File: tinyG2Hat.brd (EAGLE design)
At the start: 101.9 x 69.3 mm, 31 parts

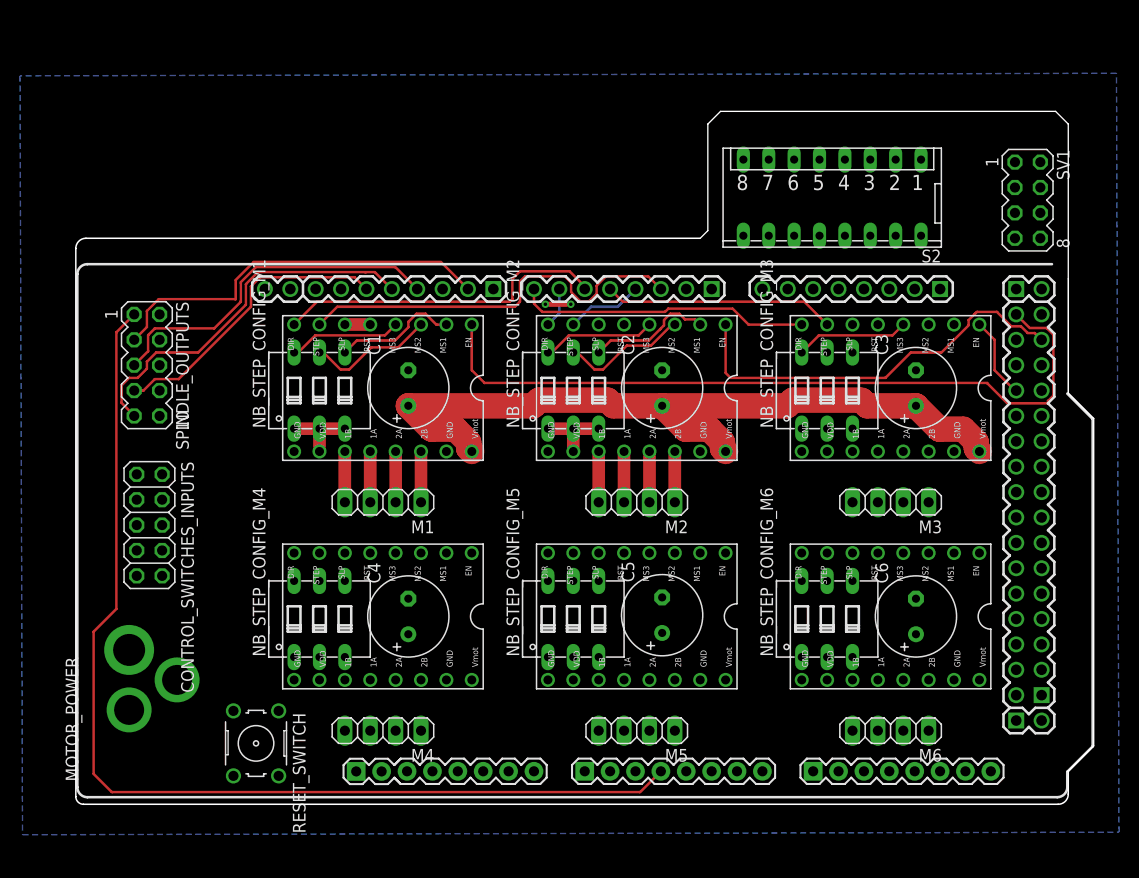
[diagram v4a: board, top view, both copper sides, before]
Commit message: Routage de M3 et des entrées avec leur switch de config
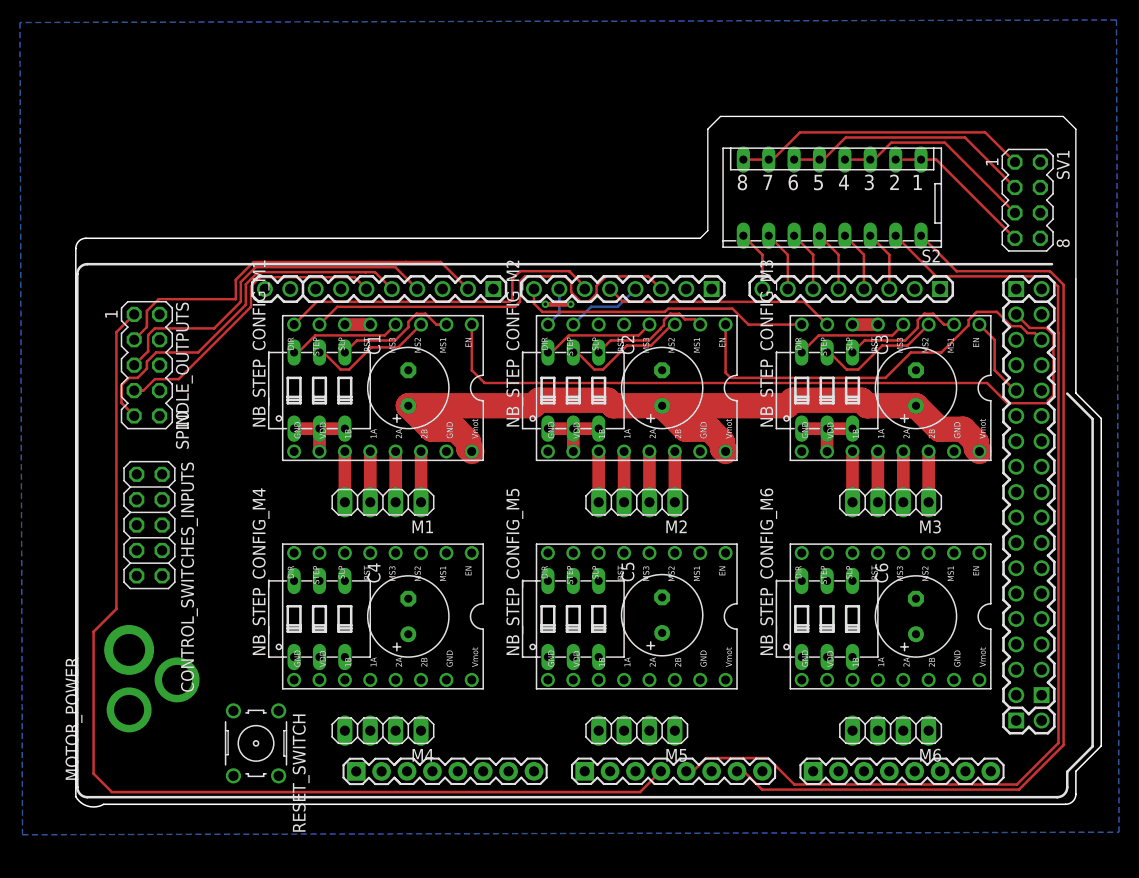
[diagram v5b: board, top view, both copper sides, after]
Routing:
- net E_STOP: track 0.00 -> 104.7 mm
- net H_INTERLCK: track 0.00 -> 97.6 mm
- net N$55: track 0.00 -> 29.5 mm
- net N$53: track 0.00 -> 25.1 mm
- net N$51: track 0.00 -> 20.6 mm
- net N$49: track 0.00 -> 15.2 mm
- net N$17: track 0.00 -> 12.7 mm
- net N$24: track 0.00 -> 12.7 mm
- net +3V3: track 14.7 -> 22.1 mm
- net Z_MIN: track 0.00 -> 6.12 mm
- net Z_MAX: track 0.00 -> 6.12 mm
- net Y_MIN: track 0.00 -> 6.12 mm
- net X_MIN: track 0.00 -> 6.12 mm
- net X_MAX: track 0.00 -> 6.12 mm
- net Y_MAX: track 0.00 -> 6.12 mm
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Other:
- board size 101.9 x 69.3 mm -> 102.6 x 69.1 mm

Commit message: Routage de M4
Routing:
- net M4_STEP: track 0.00 -> 79.0 mm
- net M4_DIR: track 0.00 -> 76.9 mm
- net +24V: track 77.5 -> 148.2 mm, vias 0 -> 2
- net M4_ENABLE: track 0.00 -> 62.6 mm
- net N$25: track 0.00 -> 12.7 mm
- net N$32: track 0.00 -> 12.5 mm
- net N$31: track 0.00 -> 11.3 mm
- net +3V3: track 22.1 -> 29.5 mm
- net N$30: track 0.00 -> 5.08 mm
- net N$29: track 0.00 -> 5.08 mm
- net N$28: track 0.00 -> 5.08 mm
- net N$27: track 0.00 -> 5.08 mm
- net N$26: track 0.00 -> 2.54 mm
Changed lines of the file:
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@@
 <attribute name="SPICEPREFIX" value="C" x="72.39" y="22.86" size="1.778" layer="27" rot="R90" display="off"/>
 </element>
-<element name="U$4" library="RepRapjr" package="A4988BREAKOUT" value="A4988BREAKOUT" x="38.1" y="13.97" rot="R180"/>
+<element name="U$4" library="RepRapjr" package="A4988BREAKOUT" value="A4988BREAKOUT" x="38.1" y="13.97" smashed="yes" rot="R180"/>
 <element name="NB_STEP_CONFIG_M4" library="switch-dil" library_urn="urn:adsk.eagle:library:375" package="DIP03YL" package3d_urn="urn:adsk.eagle:package:27256/2" value="" x="24.13" y="18.796">
 <attribute name="MF" value="" x="5.08" y="20.066" size="1.778" layer="27" display="off"/>
@@
 <contactref element="ARDUINO_DUE1" pad="32"/>
 <contactref element="U$4" pad="DIR"/>
-<wire x1="21.59" y1="25.4" x2="93.853" y2="36.576" width="0" layer="19" extent="1-1"/>
+<wire x1="21.59" y1="25.4" x2="24.638" y2="28.448" width="0.254" layer="1"/>
+<wire x1="85.725" y1="28.448" x2="93.853" y2="36.576" width="0.254" layer="1"/>
+<wire x1="24.638" y1="28.448" x2="85.725" y2="28.448" width="0.254" layer="1"/>
 </signal>
 <signal name="M1_VREF">
@@
 <contactref element="ARDUINO_DUE1" pad="31"/>
 <contactref element="U$4" pad="STEP"/>
-<wire x1="24.13" y1="25.4" x2="96.393" y2="39.116" width="0" layer="19" extent="1-1"/>
+<wire x1="24.13" y1="25.4" x2="26.67" y2="27.94" width="0.254" layer="1"/>
+<wire x1="96.266" y1="39.116" x2="96.393" y2="39.116" width="0.254" layer="1"/>
+<wire x1="93.390325" y1="35.3949" x2="94.34223125" y2="35.3949" width="0.254" layer="1"/>
+<wire x1="94.34223125" y1="35.3949" x2="95.0341" y2="36.08676875" width="0.254" layer="1"/>
+<wire x1="85.935425" y1="27.94" x2="93.390325" y2="35.3949" width="0.254" layer="1"/>
+<wire x1="95.0341" y1="37.8841" x2="96.266" y2="39.116" width="0.254" layer="1"/>
+<wire x1="95.0341" y1="36.08676875" x2="95.0341" y2="37.8841" width="0.254" layer="1"/>
+<wire x1="26.67" y1="27.94" x2="85.935425" y2="27.94" width="0.254" layer="1"/>
 </signal>
 <signal name="M4_ENABLE">
 <contactref element="ARDUINO_DUE1" pad="33"/>
 <contactref element="U$4" pad="EN"/>
-<wire x1="39.37" y1="25.4" x2="96.393" y2="36.576" width="0" layer="19" extent="1-1"/>
+<wire x1="39.37" y1="25.4" x2="41.402" y2="27.432" width="0.254" layer="1"/>
+<wire x1="41.402" y1="27.432" x2="86.14585" y2="27.432" width="0.254" layer="1"/>
+<wire x1="94.34223125" y1="32.8549" x2="95.0341" y2="33.54676875" width="0.254" layer="1"/>
+<wire x1="86.14585" y1="27.432" x2="91.56875" y2="32.8549" width="0.254" layer="1"/>
+<wire x1="91.56875" y1="32.8549" x2="94.34223125" y2="32.8549" width="0.254" layer="1"/>
+<wire x1="95.0341" y1="33.54676875" x2="95.0341" y2="35.2171" width="0.254" layer="1"/>
+<wire x1="95.0341" y1="35.2171" x2="96.393" y2="36.576" width="0.254" layer="1"/>
 </signal>
 <signal name="M4_MS0">
@@
 <wire x1="74.93" y1="37.846" x2="77.47" y2="37.846" width="1.27" layer="1"/>
 <wire x1="74.93" y1="37.846" x2="74.93" y2="35.56" width="1.27" layer="1"/>
+<wire x1="21.59" y1="14.986" x2="24.13" y2="14.986" width="1.27" layer="1"/>
+<wire x1="24.13" y1="14.986" x2="26.67" y2="14.986" width="1.27" layer="1"/>
+<wire x1="24.13" y1="14.986" x2="24.13" y2="12.7" width="1.27" layer="1"/>
 <wire x1="52.07" y1="37.846" x2="72.39" y2="37.846" width="0" layer="19" extent="1-1"/>
 <wire x1="26.67" y1="37.846" x2="46.99" y2="37.846" width="0" layer="19" extent="1-1"/>
@@
 <wire x1="35.433" y1="3.556" x2="46.99" y2="14.986" width="0" layer="19" extent="1-1"/>
 <wire x1="26.67" y1="14.986" x2="35.433" y2="3.556" width="0" layer="19" extent="1-1"/>
-<wire x1="24.13" y1="14.986" x2="26.67" y2="14.986" width="0" layer="19" extent="1-1"/>
-<wire x1="24.13" y1="12.7" x2="24.13" y2="14.986" width="0" layer="19" extent="1-1"/>
-<wire x1="21.59" y1="14.986" x2="24.13" y2="14.986" width="0" layer="19" extent="1-1"/>
 </signal>
 <signal name="+5V">
@@
 <wire x1="39.058" y1="35.872" x2="39.37" y2="35.56" width="2.54" layer="1"/>
 <wire x1="35.364" y1="37.788" x2="37.75286875" y2="37.788" width="2.54" layer="1"/>
+<wire x1="37.75286875" y1="14.928" x2="39.058" y2="13.62286875" width="2.54" layer="1"/>
+<wire x1="33.02" y1="17.272" x2="35.364" y2="14.928" width="2.54" layer="1"/>
+<wire x1="39.058" y1="13.62286875" x2="39.058" y2="13.012" width="2.54" layer="1"/>
+<wire x1="39.058" y1="13.012" x2="39.37" y2="12.7" width="2.54" layer="1"/>
+<wire x1="35.364" y1="14.928" x2="37.75286875" y2="14.928" width="2.54" layer="1"/>
+<wire x1="5.08" y1="9.7" x2="6.398" y2="8.382" width="2.54" layer="1"/>
+<wire x1="13.654" y1="11.13675625" x2="13.654" y2="11.368" width="2.54" layer="1"/>
+<wire x1="13.654" y1="11.368" x2="13.716" y2="11.43" width="2.54" layer="1"/>
+<wire x1="10.89924375" y1="8.382" x2="13.654" y2="11.13675625" width="2.54" layer="1"/>
+<wire x1="6.398" y1="8.382" x2="10.89924375" y2="8.382" width="2.54" layer="1"/>
+<wire x1="13.716" y1="11.43" x2="13.716" y2="15.24" width="2.54" layer="1"/>
+<wire x1="32.258" y1="18.034" x2="33.02" y2="17.272" width="2.54" layer="1"/>
+<wire x1="13.716" y1="15.24" x2="16.51" y2="18.034" width="2.54" layer="1"/>
+<wire x1="16.51" y1="18.034" x2="32.258" y2="18.034" width="2.54" layer="1"/>
+<wire x1="33.02" y1="17.272" x2="37.592" y2="21.844" width="2.54" layer="1"/>
+<wire x1="37.592" y1="21.844" x2="40.894" y2="21.844" width="2.54" layer="1"/>
+<wire x1="40.894" y1="21.844" x2="43.688" y2="24.638" width="2.54" layer="1"/>
+<via x="43.688" y="24.638" extent="1-16" drill="0.35"/>
+<wire x1="43.688" y1="24.638" x2="43.688" y2="30.734" width="2.54" layer="16"/>
+<via x="43.688" y="30.734" extent="1-16" drill="0.35"/>
+<wire x1="43.688" y1="30.734" x2="39.058" y2="35.364" width="2.54" layer="1"/>
+<wire x1="39.058" y1="35.364" x2="39.058" y2="35.872" width="2.54" layer="1"/>
 <wire x1="83.82" y1="17.272" x2="90.17" y2="12.7" width="0" layer="19" extent="1-1"/>
 <wire x1="90.17" y1="35.56" x2="83.82" y2="17.272" width="0" layer="19" extent="1-1"/>
-<wire x1="58.42" y1="17.399" x2="64.77" y2="35.56" width="0" layer="19" extent="1-1"/>
+<wire x1="58.42" y1="17.399" x2="43.688" y2="24.638" width="0" layer="19" extent="16-16"/>
 <wire x1="64.77" y1="12.7" x2="58.42" y2="17.399" width="0" layer="19" extent="1-1"/>
-<wire x1="33.02" y1="17.272" x2="39.37" y2="35.56" width="0" layer="19" extent="1-1"/>
-<wire x1="39.37" y1="12.7" x2="33.02" y2="17.272" width="0" layer="19" extent="1-1"/>
-<wire x1="5.08" y1="9.7" x2="33.02" y2="17.272" width="0" layer="19" extent="1-1"/>
 </signal>
 <signal name="N$9">
@@
 <contactref element="NB_STEP_CONFIG_M4" pad="5"/>
 <contactref element="U$4" pad="MS2"/>
-<wire x1="24.13" y1="22.606" x2="34.29" y2="25.4" width="0" layer="19" extent="1-1"/>
+<wire x1="34.29" y1="25.4" x2="32.189" y2="23.299" width="0.254" layer="1"/>
+<wire x1="27.1013625" y1="20.9042" x2="26.2386375" y2="20.9042" width="0.254" layer="1"/>
+<wire x1="29.4961625" y1="23.299" x2="27.1013625" y2="20.9042" width="0.254" layer="1"/>
+<wire x1="32.189" y1="23.299" x2="29.4961625" y2="23.299" width="0.254" layer="1"/>
+<wire x1="24.5368375" y1="22.606" x2="24.13" y2="22.606" width="0.254" layer="1"/>
+<wire x1="26.2386375" y1="20.9042" x2="24.5368375" y2="22.606" width="0.254" layer="1"/>
 </signal>
 <signal name="N$26">
 <contactref element="U$4" pad="RST"/>
 <contactref element="U$4" pad="SLP"/>
-<wire x1="26.67" y1="25.4" x2="29.21" y2="25.4" width="0" layer="19" extent="1-1"/>
+<wire x1="26.67" y1="25.4" x2="29.21" y2="25.4" width="1.27" layer="1"/>
 </signal>
 <signal name="N$27">
 <contactref element="U$4" pad="2B"/>
 <contactref element="M4" pad="1"/>
-<wire x1="34.29" y1="7.62" x2="34.29" y2="12.7" width="0" layer="19" extent="1-1"/>
+<wire x1="34.29" y1="12.7" x2="34.29" y2="7.62" width="1.27" layer="1"/>
 </signal>
 <signal name="N$28">
 <contactref element="U$4" pad="2A"/>
 <contactref element="M4" pad="2"/>
-<wire x1="31.75" y1="7.62" x2="31.75" y2="12.7" width="0" layer="19" extent="1-1"/>
+<wire x1="31.75" y1="12.7" x2="31.75" y2="7.62" width="1.27" layer="1"/>
 </signal>
 <signal name="N$29">
 <contactref element="U$4" pad="1A"/>
 <contactref element="M4" pad="3"/>
-<wire x1="29.21" y1="7.62" x2="29.21" y2="12.7" width="0" layer="19" extent="1-1"/>
+<wire x1="29.21" y1="12.7" x2="29.21" y2="7.62" width="1.27" layer="1"/>
 </signal>
 <signal name="N$30">
 <contactref element="U$4" pad="1B"/>
 <contactref element="M4" pad="4"/>
-<wire x1="26.67" y1="7.62" x2="26.67" y2="12.7" width="0" layer="19" extent="1-1"/>
+<wire x1="26.67" y1="12.7" x2="26.67" y2="7.62" width="1.27" layer="1"/>
 </signal>
 <signal name="N$31">
 <contactref element="U$4" pad="MS3"/>
 <contactref element="NB_STEP_CONFIG_M4" pad="6"/>
-<wire x1="21.59" y1="22.606" x2="31.75" y2="25.4" width="0" layer="19" extent="1-1"/>
+<wire x1="21.59" y1="22.606" x2="23.299" y2="24.315" width="0.254" layer="1"/>
+<wire x1="30.665" y1="24.315" x2="31.75" y2="25.4" width="0.254" layer="1"/>
+<wire x1="23.299" y1="24.315" x2="30.665" y2="24.315" width="0.254" layer="1"/>
 </signal>
 <signal name="N$32">
 <contactref element="NB_STEP_CONFIG_M4" pad="4"/>
 <contactref element="U$4" pad="MS1"/>
-<wire x1="26.67" y1="22.606" x2="36.83" y2="25.4" width="0" layer="19" extent="1-1"/>
+<wire x1="33.840575" y1="26.485" x2="34.739425" y2="26.485" width="0.254" layer="1"/>
+<wire x1="36.83" y1="25.4" x2="35.824425" y2="25.4" width="0.254" layer="1"/>
+<wire x1="35.824425" y1="25.4" x2="34.739425" y2="26.485" width="0.254" layer="1"/>
+<wire x1="31.691425" y1="23.807" x2="32.835" y2="24.950575" width="0.254" layer="1"/>
+<wire x1="27.871" y1="23.807" x2="26.67" y2="22.606" width="0.254" layer="1"/>
+<wire x1="31.691425" y1="23.807" x2="27.871" y2="23.807" width="0.254" layer="1"/>
+<wire x1="32.835" y1="24.950575" x2="32.835" y2="25.479425" width="0.254" layer="1"/>
+<wire x1="32.835" y1="25.479425" x2="33.840575" y2="26.485" width="0.254" layer="1"/>
 </signal>
 <signal name="N$33">

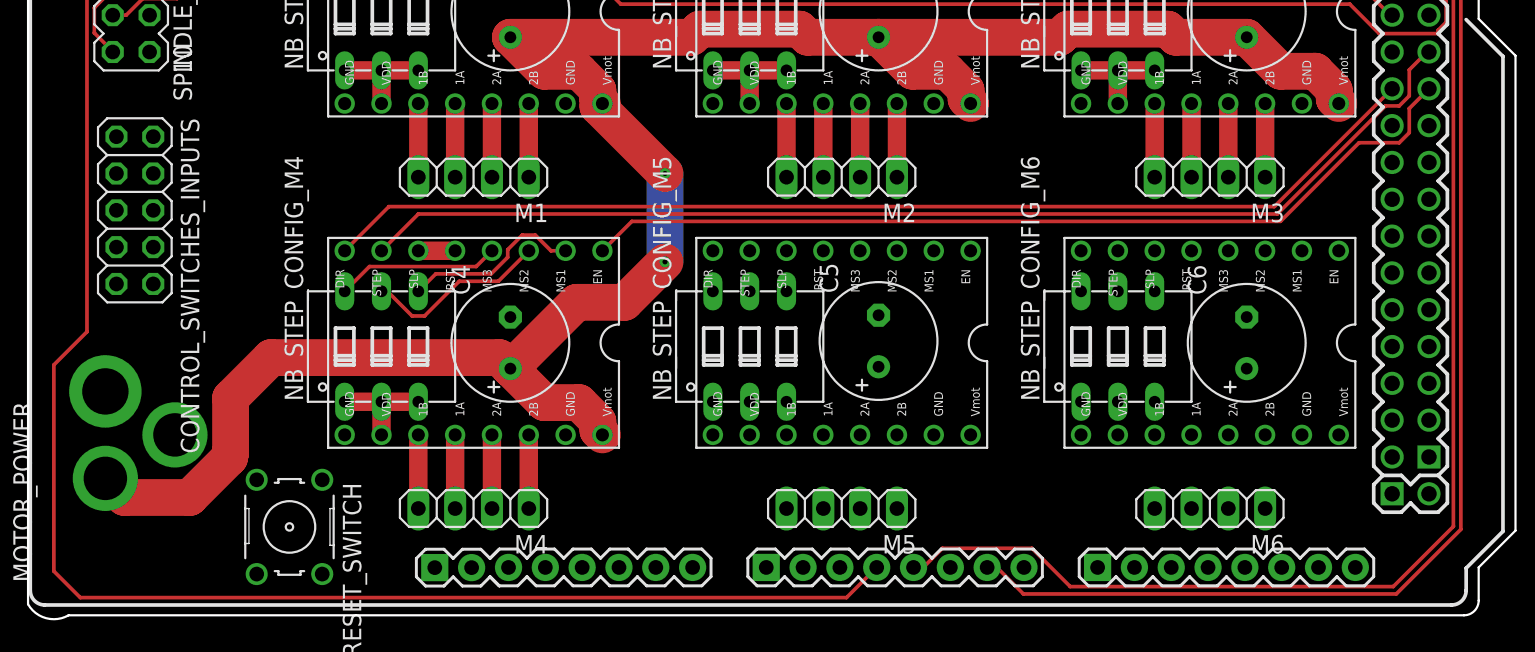
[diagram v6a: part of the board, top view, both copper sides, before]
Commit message: Routage de M5 et M6. 6 drivers, spindle, 4 capteurs routés
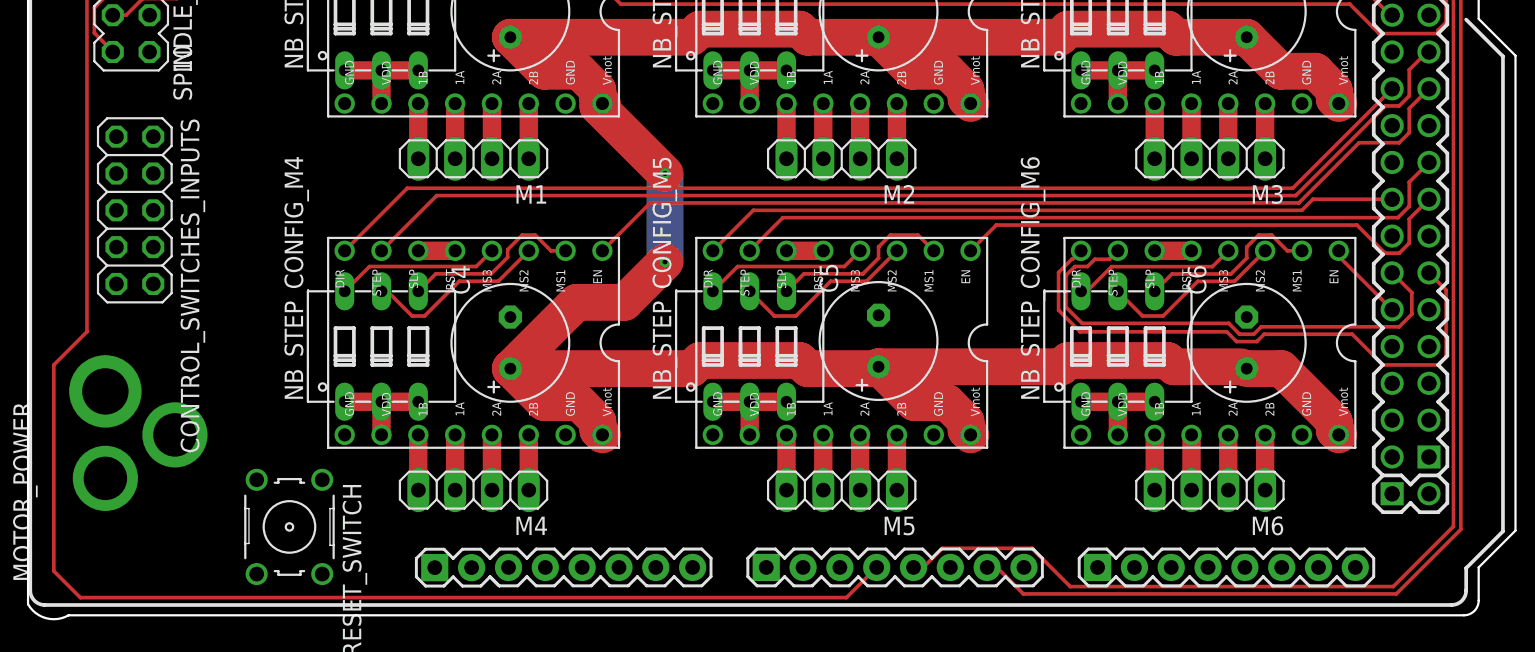
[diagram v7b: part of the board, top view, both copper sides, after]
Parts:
- moved M4 1.27 mm to (30.5, 8.89)
- moved M5 1.27 mm to (55.9, 8.89)
- moved M6 1.27 mm to (81.3, 8.89)
- moved M1 1.27 mm to (30.5, 31.8)
- moved M2 1.27 mm to (55.9, 31.8)
- moved M3 1.27 mm to (81.3, 31.8)
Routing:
- net M5_STEP: track 0.00 -> 50.4 mm
- net M5_DIR: track 0.00 -> 48.3 mm
- net M6_DIR: track 0.00 -> 40.0 mm
- net M5_ENABLE: track 0.00 -> 35.7 mm
- net M6_STEP: track 0.00 -> 35.1 mm
- net +24V: track 148.2 -> 181.6 mm
- net +3V3: track 29.5 -> 44.2 mm
- net N$41: track 0.00 -> 12.7 mm
- net N$33: track 0.00 -> 12.7 mm
- net N$40: track 0.00 -> 12.7 mm
- net N$48: track 0.00 -> 12.7 mm
- net N$47: track 0.00 -> 11.3 mm
- net N$39: track 0.00 -> 11.3 mm
- net M6_ENABLE: track 0.00 -> 5.59 mm
- net N$46: track 0.00 -> 3.81 mm
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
